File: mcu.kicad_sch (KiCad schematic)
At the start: 44 parts, among them J1 10118193-0001LF, J5 Conn_ARM_SWD_TagConnect_TC2030, SW1 SW_Push, SW2 SW_Push, SW3 SW_Push, U1 RP2040, U2 AP2112K-3.3TRG1, U3 W25Q16JVSSIQ, Y3 12MHZ

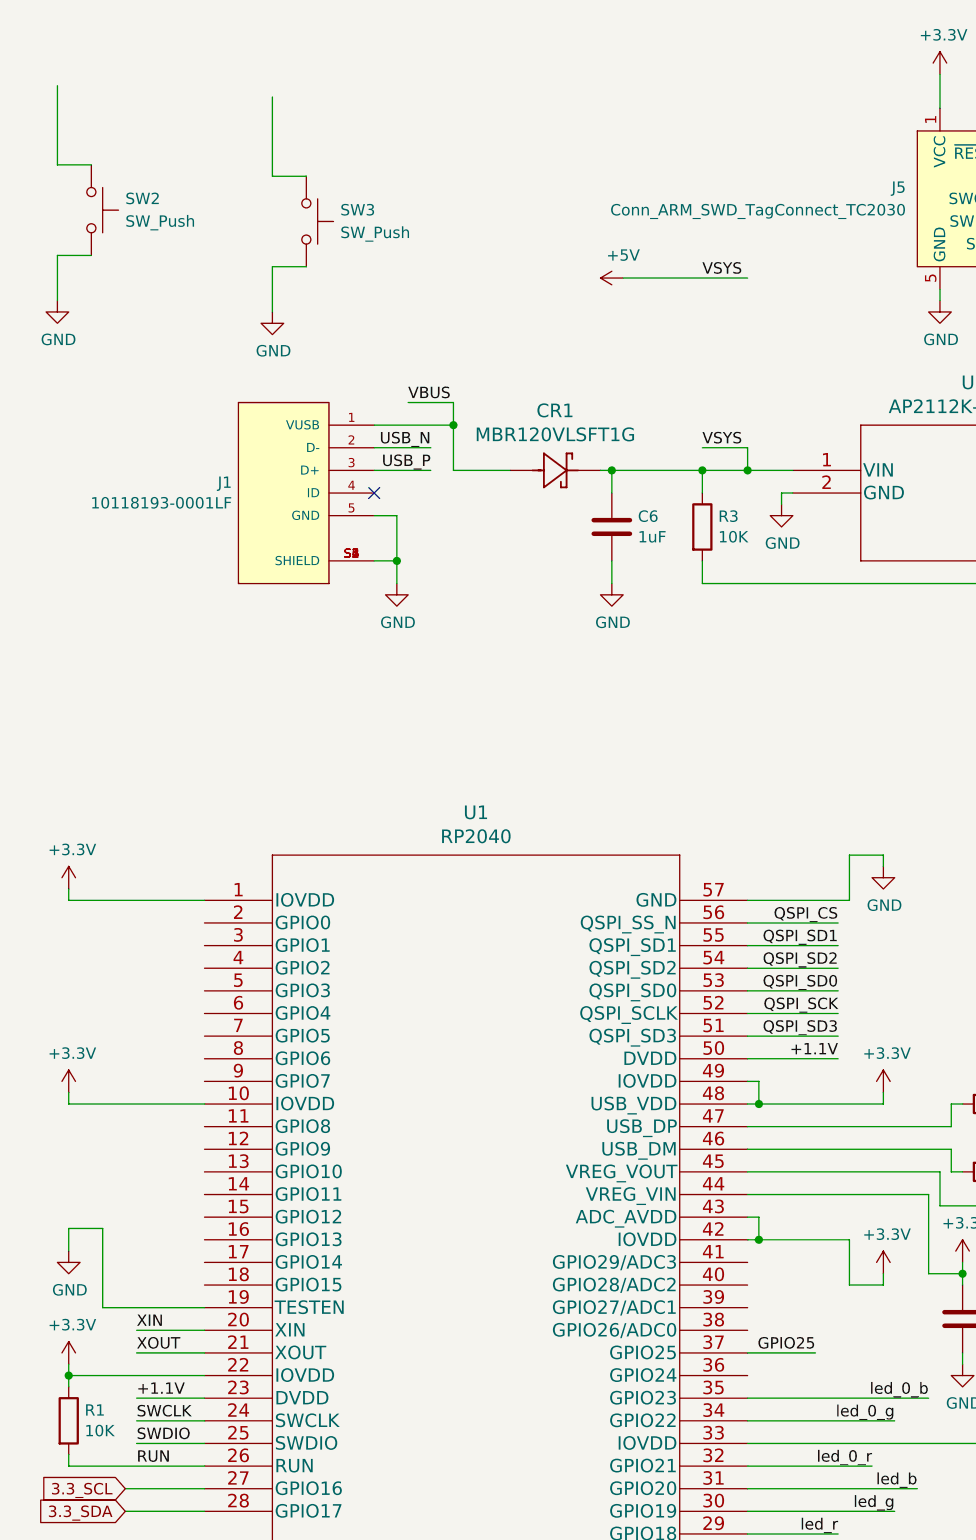
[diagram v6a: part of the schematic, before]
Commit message: Reroute i2c, connect user buttons
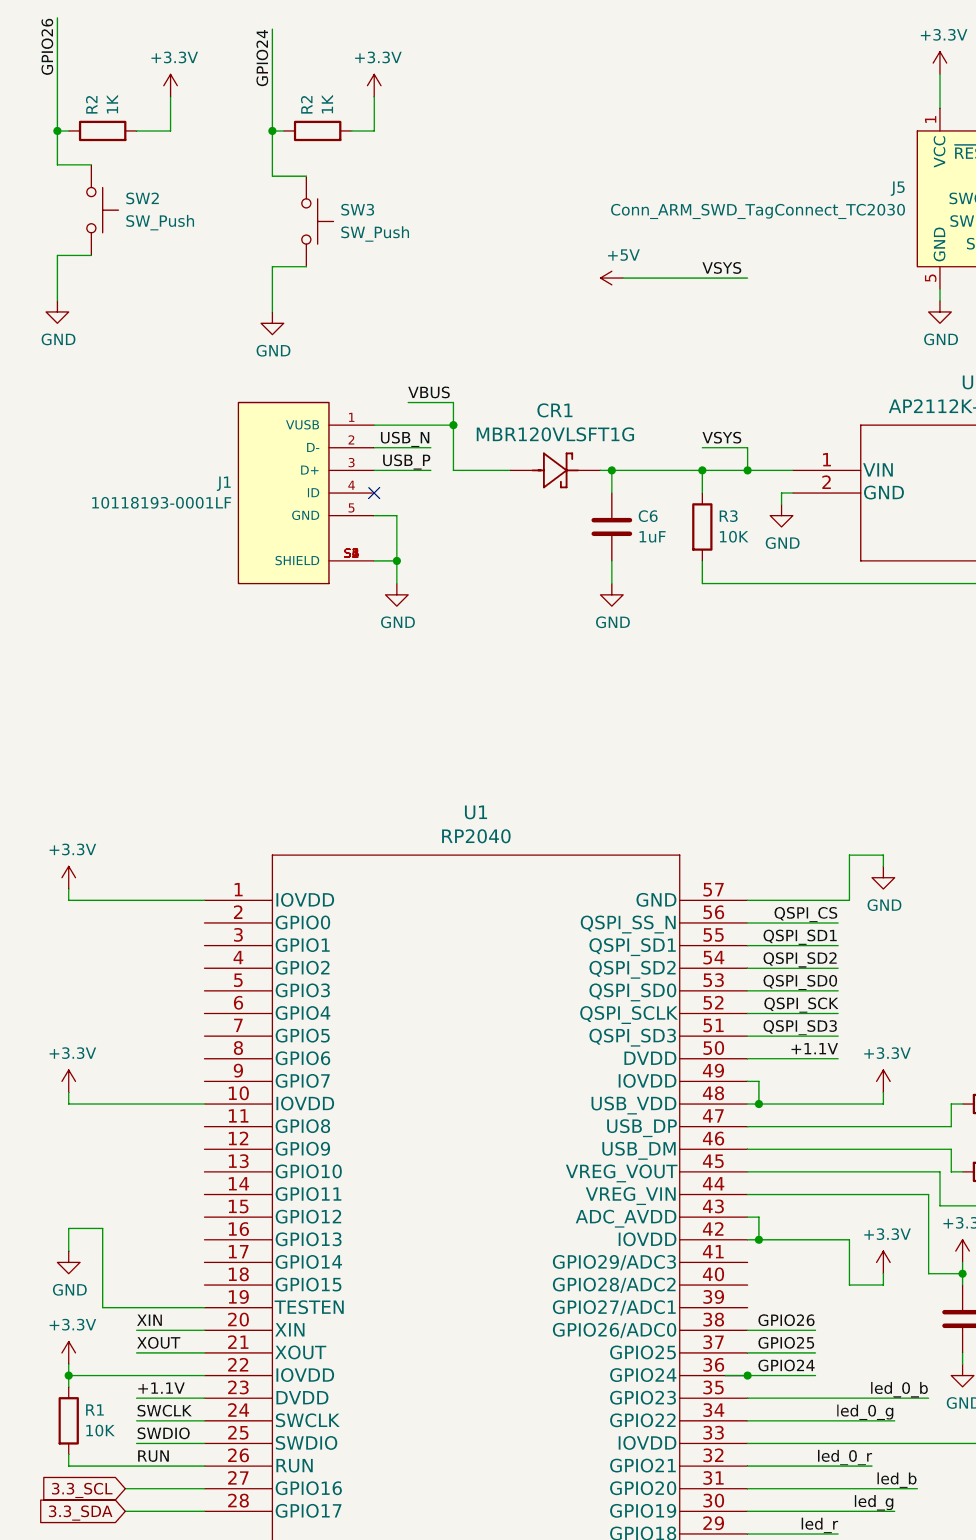
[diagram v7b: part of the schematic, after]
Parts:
- added R2 (x2): 1K, Resistor_SMD:R_0402_1005Metric, symbol Device:R
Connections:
- net +3V3: now also R2.2, R2.2
- net GPIO26: now reaches SW2.1
- net GPIO26: now also U1.38 (GPIO26/ADC0), R2.1
- net GPIO24: now reaches SW3.1
- net GPIO24: now also U1.36 (GPIO24), R2.1
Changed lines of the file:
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@@
   (junction (at 167.64 165.1) (diameter 0) (color 0 0 0 0)
   )
+  (junction (at 22.86 25.4) (diameter 0) (color 0 0 0 0)
+  )
   (junction (at 149.86 153.67) (diameter 0) (color 0 0 0 0)
   )
@@
   (junction (at 167.64 153.67) (diameter 0) (color 0 0 0 0)
   )
+  (junction (at 100.33 165.1) (diameter 0) (color 0 0 0 0)
+  )
   (junction (at 153.67 63.5) (diameter 0) (color 0 0 0 0)
   )
@@
   (junction (at 101.6 134.62) (diameter 0) (color 0 0 0 0)
   )
+  (junction (at 46.99 25.4) (diameter 0) (color 0 0 0 0)
+  )
   (junction (at 124.46 153.67) (diameter 0) (color 0 0 0 0)
   )
@@
     (stroke (width 0) (type default))
   )
+  (wire (pts (xy 22.86 25.4) (xy 24.13 25.4))
+    (stroke (width 0) (type default))
+  )
   (wire (pts (xy 100.33 180.34) (xy 116.84 180.34))
     (stroke (width 0) (type default))
@@
     (stroke (width 0) (type default))
   )
+  (wire (pts (xy 100.33 160.02) (xy 107.95 160.02))
+    (stroke (width 0) (type default))
+  )
   (wire (pts (xy 100.33 162.56) (xy 107.95 162.56))
     (stroke (width 0) (type default))
@@
     (stroke (width 0) (type default))
   )
+  (wire (pts (xy 100.33 165.1) (xy 107.95 165.1))
+    (stroke (width 0) (type default))
+  )
   (wire (pts (xy 163.83 170.18) (xy 158.75 170.18))
     (stroke (width 0) (type default))
@@
     (stroke (width 0) (type default))
   )
-  (wire (pts (xy 46.99 21.59) (xy 46.99 30.48))
+  (wire (pts (xy 46.99 25.4) (xy 48.26 25.4))
+    (stroke (width 0) (type default))
+  )
+  (wire (pts (xy 46.99 13.97) (xy 46.99 25.4))
     (stroke (width 0) (type default))
   )
@@
     (stroke (width 0) (type default))
   )
-  (wire (pts (xy 22.86 20.32) (xy 22.86 29.21))
+  (wire (pts (xy 22.86 12.7) (xy 22.86 25.4))
     (stroke (width 0) (type default))
   )
@@
     (stroke (width 0) (type default))
   )
+  (wire (pts (xy 35.56 21.59) (xy 35.56 25.4))
+    (stroke (width 0) (type default))
+  )
   (wire (pts (xy 236.22 46.99) (xy 236.22 45.72))
     (stroke (width 0) (type default))
@@
     (stroke (width 0) (type default))
   )
+  (wire (pts (xy 31.75 25.4) (xy 35.56 25.4))
+    (stroke (width 0) (type default))
+  )
   (wire (pts (xy 207.01 130.81) (xy 204.47 130.81))
     (stroke (width 0) (type default))
@@
     (stroke (width 0) (type default))
   )
+  (wire (pts (xy 97.79 165.1) (xy 100.33 165.1))
+    (stroke (width 0) (type default))
+  )
   (wire (pts (xy 121.92 43.18) (xy 121.92 44.45))
     (stroke (width 0) (type default))
@@
     (stroke (width 0) (type default))
   )
+  (wire (pts (xy 46.99 25.4) (xy 46.99 30.48))
+    (stroke (width 0) (type default))
+  )
+  (wire (pts (xy 58.42 21.59) (xy 58.42 25.4))
+    (stroke (width 0) (type default))
+  )
+  (wire (pts (xy 22.86 25.4) (xy 22.86 29.21))
+    (stroke (width 0) (type default))
+  )
   (wire (pts (xy 153.67 73.66) (xy 153.67 76.2))
     (stroke (width 0) (type default))
@@
     (stroke (width 0) (type default))
   )
+  (wire (pts (xy 55.88 25.4) (xy 58.42 25.4))
+    (stroke (width 0) (type default))
+  )
   (text "BOOTSEL" (at 267.97 45.72 0)
     (effects (font (size 1.27 1.27)) (justify left bottom))
@@
     (effects (font (size 1.27 1.27)) (justify right bottom))
   )
+  (label "GPIO24" (at 46.99 13.97 270) (fields_autoplaced)
+    (effects (font (size 1.27 1.27)) (justify right bottom))
+  )
   (label "VSYS" (at 95.25 41.91 0) (fields_autoplaced)
     (effects (font (size 1.27 1.27)) (justify left bottom))
@@
     (effects (font (size 1.27 1.27)) (justify right bottom))
   )
+  (label "GPIO26" (at 107.95 160.02 180) (fields_autoplaced)
+    (effects (font (size 1.27 1.27)) (justify right bottom))
+  )
   (label "SWDIO" (at 138.43 35.56 0) (fields_autoplaced)
     (effects (font (size 1.27 1.27)) (justify left bottom))
@@
     (effects (font (size 1.27 1.27)) (justify left bottom))
   )
+  (label "GPIO26" (at 22.86 12.7 270) (fields_autoplaced)
+    (effects (font (size 1.27 1.27)) (justify right bottom))
+  )
   (label "GPIO25" (at 107.95 162.56 180) (fields_autoplaced)
     (effects (font (size 1.27 1.27)) (justify right bottom))
@@
     (effects (font (size 1.27 1.27)) (justify left bottom))
   )
+  (label "GPIO24" (at 107.95 165.1 180) (fields_autoplaced)
+    (effects (font (size 1.27 1.27)) (justify right bottom))
+  )
   (label "QSPI_SD0" (at 110.49 121.92 180) (fields_autoplaced)
     (effects (font (size 1.27 1.27)) (justify right bottom))
@@
     )
   )
+  (symbol (lib_id "rpi-pico-debugger-shoe-rescue:+3.3V-power") (at 35.56 21.59 0) (unit 1)
+    (in_bom yes) (on_board yes) (dnp no)
+    (property "Reference" "#PWR0104" (at 35.56 25.4 0)
+      (effects (font (size 1.27 1.27)) hide)
+    )
+    (property "Value" "+3.3V" (at 35.941 17.1958 0)
+      (effects (font (size 1.27 1.27)))
+    )
+    (property "Footprint" "" (at 35.56 21.59 0)
+      (effects (font (size 1.27 1.27)) hide)
+    )
+    (property "Datasheet" "" (at 35.56 21.59 0)
+      (effects (font (size 1.27 1.27)) hide)
+    )
+    (pin "1")
+    (instances
+      (project "rpi-pico-debugger-shoe"
+        (path "/aad74d97-f116-4a83-b498-c8cb2f4b4e35"
+          (reference "#PWR0104") (unit 1)
+        )
+      )
+      (project "ltp_kikad"
+        (path "/eed35b77-cbf9-4596-9b17-2558f81058ba/643f5372-7b7f-4a0a-9eb8-fe959bdc465c"
+          (reference "#PWR066") (unit 1)
+        )
+      )
+    )
+  )
   (symbol (lib_id "rpi-pico-debugger-shoe-rescue:+3.3V-power") (at 266.7 124.46 0) (unit 1)
     (in_bom yes) (on_board yes) (dnp no)
@@
     )
   )
+  (symbol (lib_id "Device:R") (at 27.94 25.4 90) (unit 1)
+    (in_bom yes) (on_board yes) (dnp no)
+    (property "Reference" "R2" (at 26.7716 23.622 0)
+      (effects (font (size 1.27 1.27)) (justify left))
+    )
+    (property "Value" "1K" (at 29.083 23.622 0)
+      (effects (font (size 1.27 1.27)) (justify left))
+    )
+    (property "Footprint" "Resistor_SMD:R_0402_1005Metric" (at 27.94 27.178 90)
+      (effects (font (size 1.27 1.27)) hide)
+    )
+    (property "Datasheet" "~" (at 27.94 25.4 0)
+      (effects (font (size 1.27 1.27)) hide)
+    )
+    (property "Digi-Key_PN" "311-1.00KHRCT-ND" (at 27.94 25.4 0)
+      (effects (font (size 1.27 1.27)) hide)
+    )
+    (pin "1")
+    (pin "2")
+    (instances
+      (project "rpi-pico-debugger-shoe"
+        (path "/aad74d97-f116-4a83-b498-c8cb2f4b4e35"
+          (reference "R2") (unit 1)
+        )
+      )
+      (project "ltp_kikad"
+        (path "/eed35b77-cbf9-4596-9b17-2558f81058ba/643f5372-7b7f-4a0a-9eb8-fe959bdc465c"
+          (reference "R14") (unit 1)
+        )
+      )
+    )
+  )
   (symbol (lib_id "Device:R") (at 236.22 50.8 0) (unit 1)
     (in_bom yes) (on_board yes) (dnp no)
@@
     )
   )
+  (symbol (lib_id "rpi-pico-debugger-shoe-rescue:+3.3V-power") (at 58.42 21.59 0) (unit 1)
+    (in_bom yes) (on_board yes) (dnp no)
+    (property "Reference" "#PWR0104" (at 58.42 25.4 0)
+      (effects (font (size 1.27 1.27)) hide)
+    )
+    (property "Value" "+3.3V" (at 58.801 17.1958 0)
+      (effects (font (size 1.27 1.27)))
+    )
+    (property "Footprint" "" (at 58.42 21.59 0)
+      (effects (font (size 1.27 1.27)) hide)
+    )
+    (property "Datasheet" "" (at 58.42 21.59 0)
+      (effects (font (size 1.27 1.27)) hide)
+    )
+    (pin "1")
+    (instances
+      (project "rpi-pico-debugger-shoe"
+        (path "/aad74d97-f116-4a83-b498-c8cb2f4b4e35"
+          (reference "#PWR0104") (unit 1)
+        )
+      )
+      (project "ltp_kikad"
+        (path "/eed35b77-cbf9-4596-9b17-2558f81058ba/643f5372-7b7f-4a0a-9eb8-fe959bdc465c"
+          (reference "#PWR065") (unit 1)
+        )
+      )
+    )
+  )
   (symbol (lib_id "rpi-pico-debugger-shoe-rescue:+3.3V-power") (at 129.54 167.64 0) (unit 1)
     (in_bom yes) (on_board yes) (dnp no)
@@
         )
       )
+    )
+  )
+  (symbol (lib_id "Device:R") (at 52.07 25.4 90) (unit 1)
+    (in_bom yes) (on_board yes) (dnp no)
+    (property "Reference" "R2" (at 50.9016 23.622 0)
+      (effects (font (size 1.27 1.27)) (justify left))
+    )
+    (property "Value" "1K" (at 53.213 23.622 0)
+      (effects (font (size 1.27 1.27)) (justify left))
+    )
+    (property "Footprint" "Resistor_SMD:R_0402_1005Metric" (at 52.07 27.178 90)
+      (effects (font (size 1.27 1.27)) hide)
+    )
+    (property "Datasheet" "~" (at 52.07 25.4 0)
+      (effects (font (size 1.27 1.27)) hide)
+    )
+    (property "Digi-Key_PN" "311-1.00KHRCT-ND" (at 52.07 25.4 0)
+      (effects (font (size 1.27 1.27)) hide)
+    )
+    (pin "1")
+    (pin "2")
+    (instances
+      (project "rpi-pico-debugger-shoe"
+        (path "/aad74d97-f116-4a83-b498-c8cb2f4b4e35"
+          (reference "R2") (unit 1)
+        )
+      )
+      (project "ltp_kikad"
+        (path "/eed35b77-cbf9-4596-9b17-2558f81058ba/643f5372-7b7f-4a0a-9eb8-fe959bdc465c"
+          (reference "R15") (unit 1)
+        )
+      )
